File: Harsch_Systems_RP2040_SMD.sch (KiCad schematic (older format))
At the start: 50 parts, among them J1 Jack-DC, J3 Conn_01x08_Female, J4 Conn_01x08_Female, J5 Conn_01x04_Female, J6 Conn_01x06_Female, J7 USB_A, J8 DEBUG, SW1 SW_MEC_5E, U1 XC6210B332MR, U11 TPS56339DDC, U3 RP2040, U4 W25Q32JVSSIQ_TR, Y1 12MHz

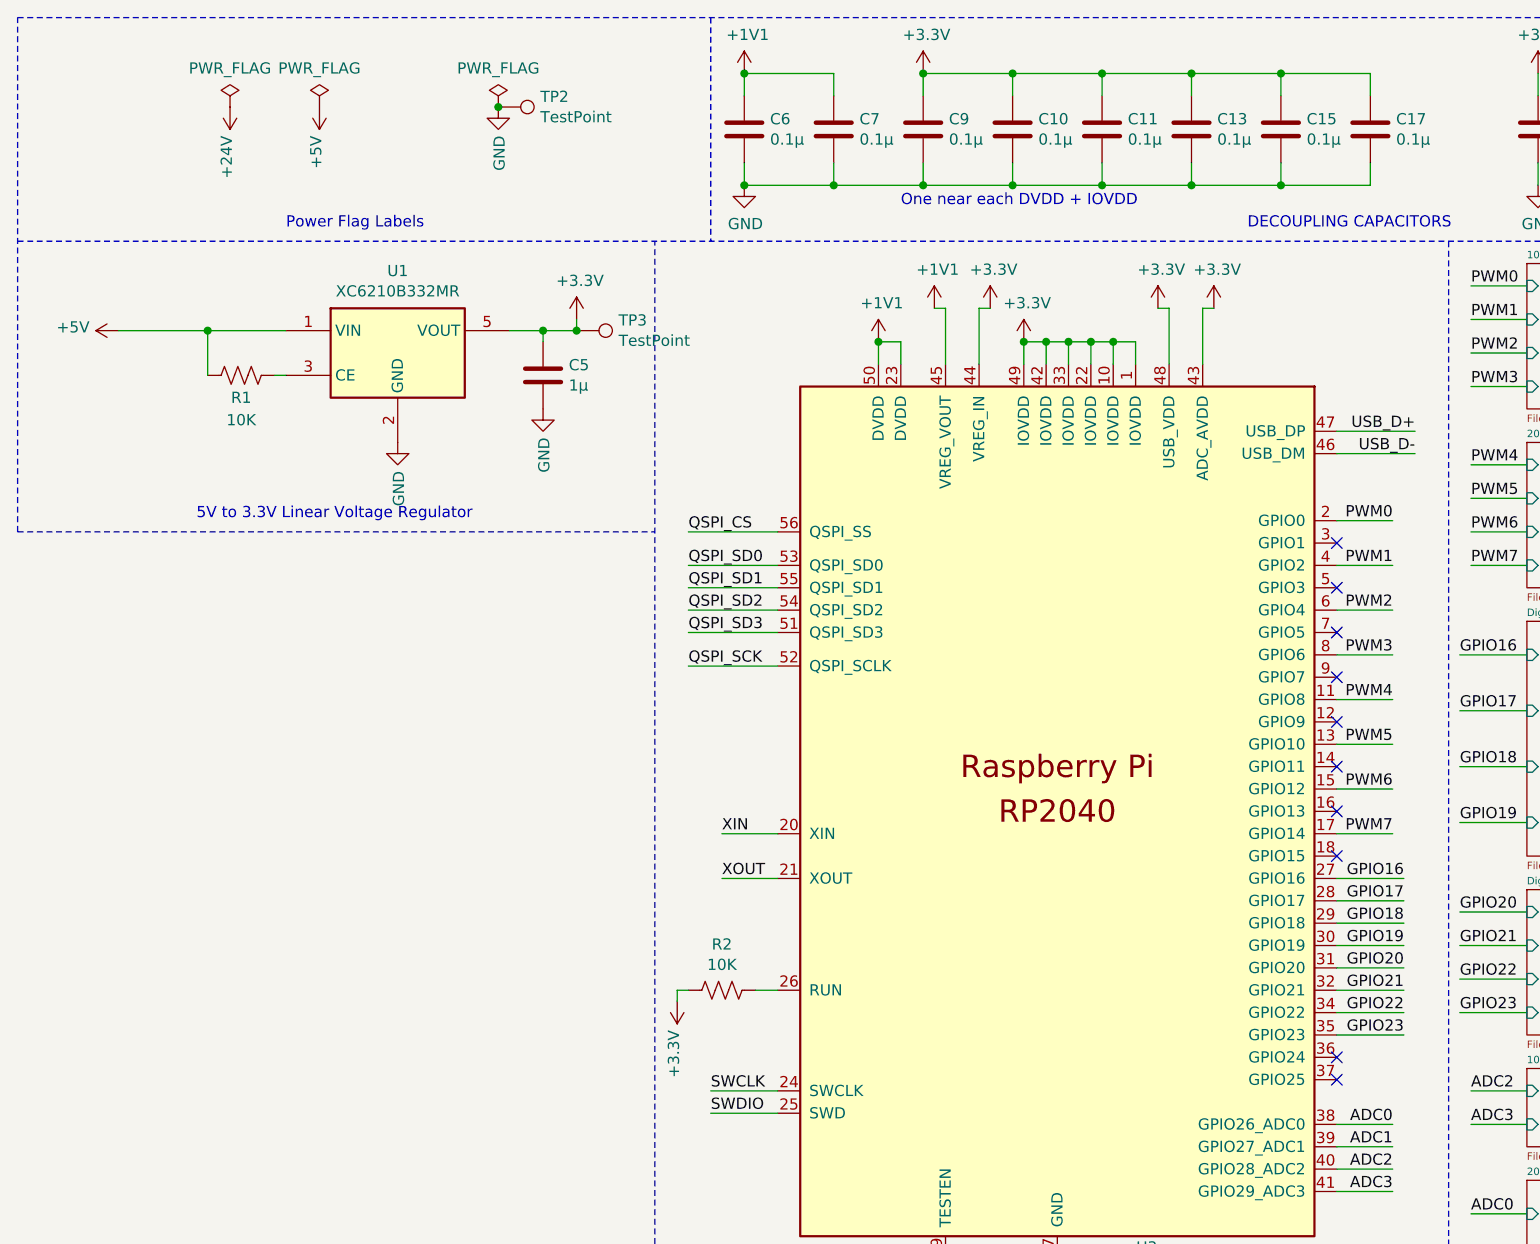
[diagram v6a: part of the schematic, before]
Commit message: Added an I2C QWIIC Connector
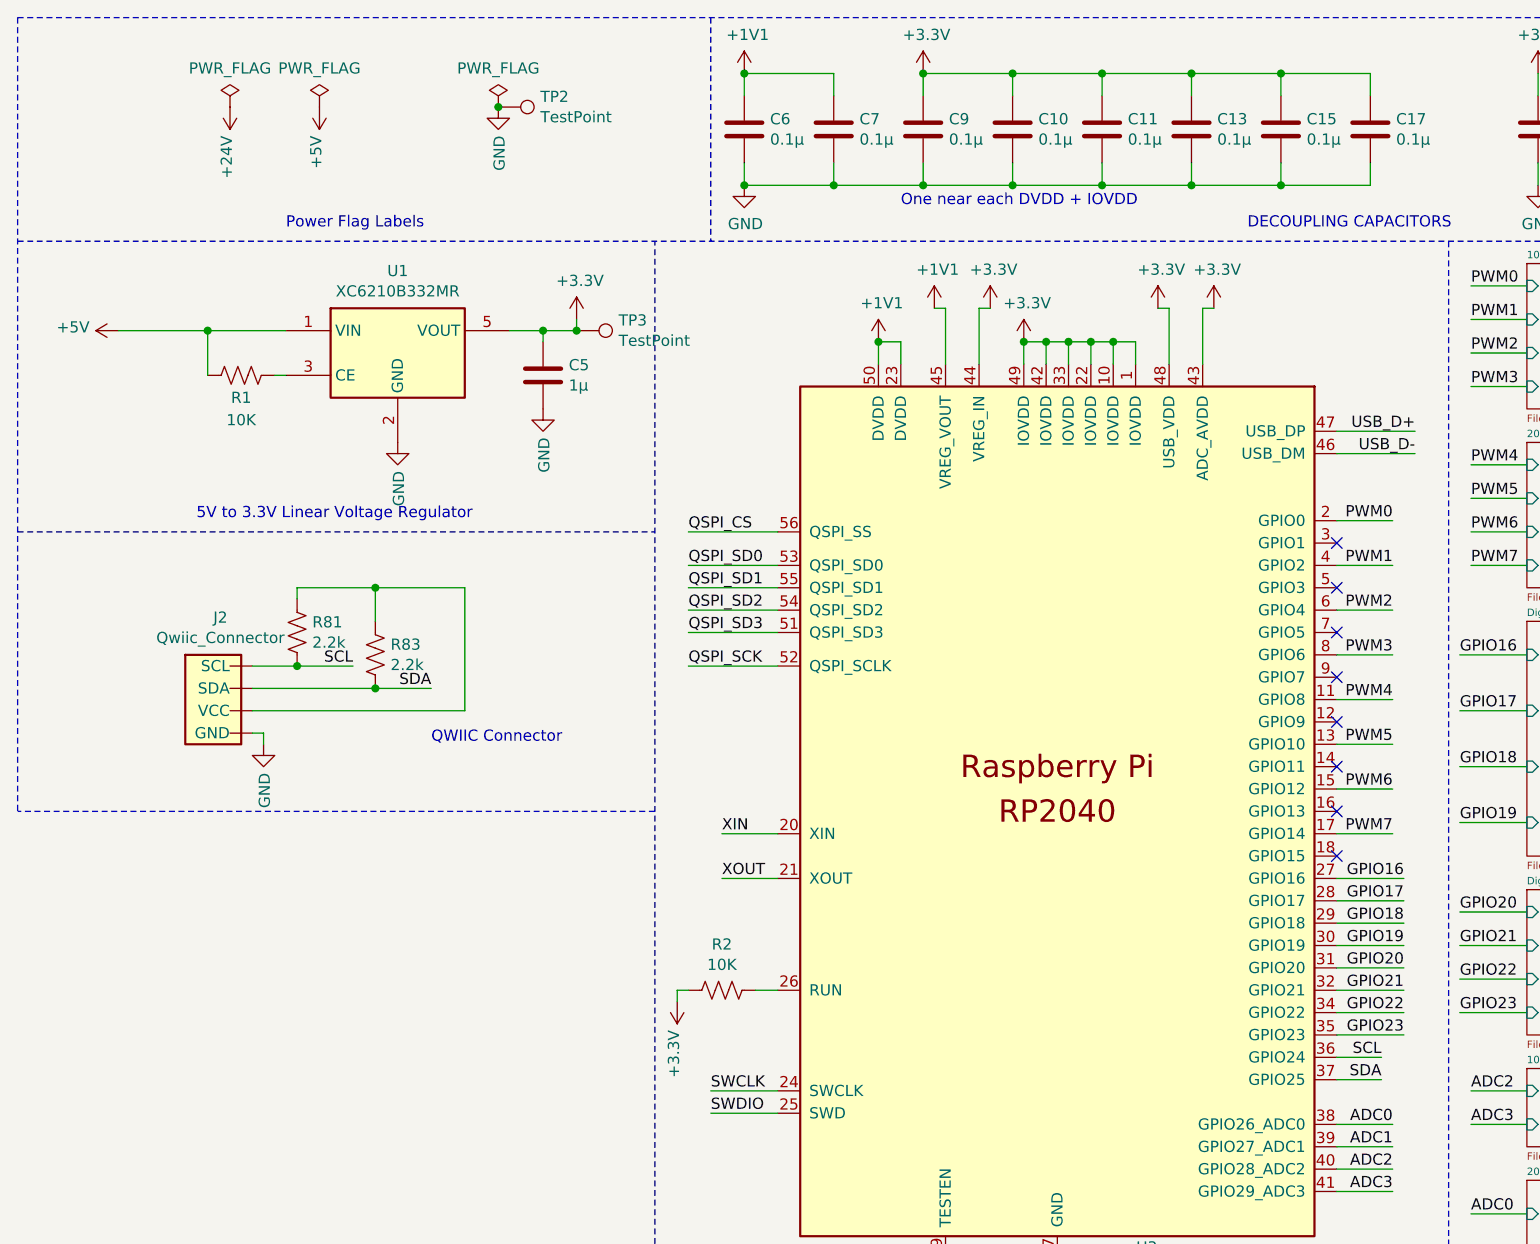
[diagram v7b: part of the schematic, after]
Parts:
- added J2: Qwiic_Connector, Connectors:1X04_1MM_RA, symbol SparkFun_SchematicComponents:Qwiic_Connector
- added R81, R83: 2.2k, Resistor_SMD:R_0805_2012Metric, symbol Device:R_US
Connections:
- net GND: now also J2.1 (GND)
- net SCL: now reaches U3.36 (GPIO24)
- net SCL: now also J2.4 (SCL), R81.2
- net SDA: now reaches U3.37 (GPIO25)
- net SDA: now also J2.3 (SDA), R83.2
- new net: J2.2 (VCC), R81.1, R83.1
- no-connect marks 12 -> 10
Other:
- note added: "QWIIC Connector"
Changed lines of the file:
@@
 Wire Wire Line
 	8400 5900 8500 5900
-NoConn ~ 6400 5150
 $Comp
 L power:PWR_FLAG #FLG04
@@
 Wire Wire Line
 	6400 4650 6700 4650
-Wire Notes Line
-	500  2800 500  500
-NoConn ~ 6400 5250
 NoConn ~ 6400 4250
 NoConn ~ 6400 4050
@@
 Wire Wire Line
 	2100 6850 2450 6850
+$Comp
+L SparkFun_SchematicComponents:Qwiic_Connector J2
+U 1 1 627377F0
+P 1350 3550
+F 0 "J2" H 1407 3917 50  0000 C CNN
+F 1 "Qwiic_Connector" H 1407 3826 50  0000 C CNN
+F 2 "Connectors:1X04_1MM_RA" H 1330 3650 20  0001 C CNN
+F 3 "" H 1300 3500 60  0001 C CNN
+	1    1350 3550
+	1    0    0    -1
+$EndComp
+$Comp
+L power:GND #PWR0107
+U 1 1 6276CE49
+P 1600 3750
+F 0 "#PWR0107" H 1600 3500 50  0001 C CNN
+F 1 "GND" V 1605 3622 50  0000 R CNN
+F 2 "" H 1600 3750 50  0001 C CNN
+F 3 "" H 1600 3750 50  0001 C CNN
+	1    1600 3750
+	1    0    0    -1
+$EndComp
+Wire Wire Line
+	1550 3700 1600 3700
+Wire Wire Line
+	1600 3700 1600 3750
+Text Label 6600 5150 2    50   ~ 0
+SCL
+Text Label 6600 5250 2    50   ~ 0
+SDA
+Wire Wire Line
+	6400 5150 6600 5150
+Wire Wire Line
+	6400 5250 6600 5250
+Text Label 2000 3400 2    50   ~ 0
+SCL
+Text Label 2350 3500 2    50   ~ 0
+SDA
+$Comp
+L Device:R_US R81
+U 1 1 62840E0D
+P 1750 3250
+F 0 "R81" H 1818 3296 50  0000 L CNN
+F 1 "2.2k" H 1818 3205 50  0000 L CNN
+F 2 "Resistor_SMD:R_0805_2012Metric" V 1790 3240 50  0001 C CNN
+F 3 "~" H 1750 3250 50  0001 C CNN
+	1    1750 3250
+	1    0    0    -1
+$EndComp
+$Comp
+L Device:R_US R83
+U 1 1 628417E3
+P 2100 3350
+F 0 "R83" H 2168 3396 50  0000 L CNN
+F 1 "2.2k" H 2168 3305 50  0000 L CNN
+F 2 "Resistor_SMD:R_0805_2012Metric" V 2140 3340 50  0001 C CNN
+F 3 "~" H 2100 3350 50  0001 C CNN
+	1    2100 3350
+	1    0    0    -1
+$EndComp
+Wire Wire Line
+	1550 3400 1750 3400
+Wire Wire Line
+	1750 3400 2000 3400
+Connection ~ 1750 3400
+Wire Wire Line
+	1550 3500 2100 3500
+Wire Wire Line
+	2100 3500 2350 3500
+Connection ~ 2100 3500
+Wire Wire Line
+	1750 3100 1750 3050
+Wire Wire Line
+	2100 3200 2100 3050
+Text Notes 2350 3750 0    50   ~ 0
+QWIIC Connector
+Wire Notes Line
+	3350 4050 500  4050
+Wire Notes Line
+	500  500  500  4050
+Wire Wire Line
+	1750 3050 2100 3050
+Wire Wire Line
+	1550 3600 2500 3600
+Wire Wire Line
+	2500 3600 2500 3050
+Wire Wire Line
+	2500 3050 2100 3050
+Connection ~ 2100 3050
 $EndSCHEMATC
